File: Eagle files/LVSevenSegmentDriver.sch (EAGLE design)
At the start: 20 parts, among them IC1 74HC595D

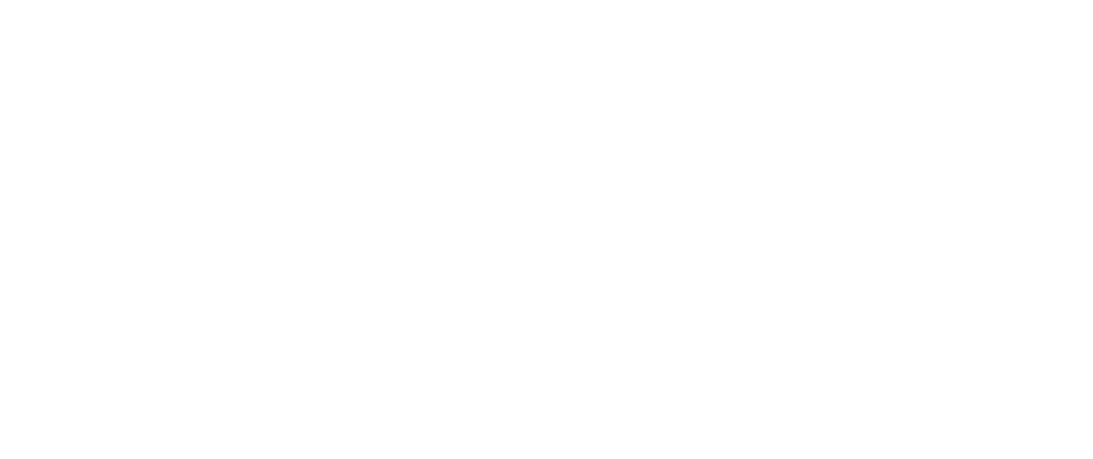
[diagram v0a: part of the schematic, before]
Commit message: Ready for Fabbing
Silk Screens added and last minute DRC checks done.
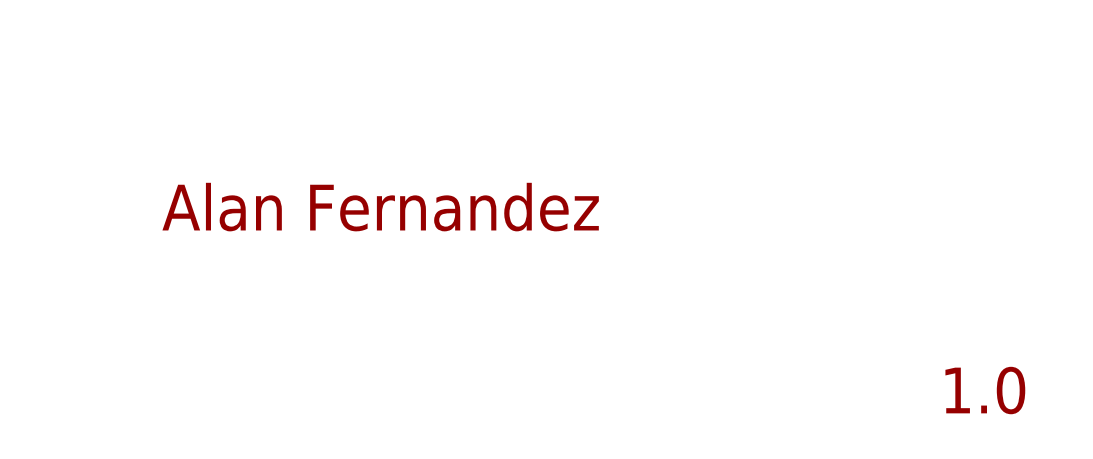
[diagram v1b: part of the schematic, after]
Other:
- note added: "1.0"
- note added: "Alan Fernandez"
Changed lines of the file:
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@@
 <part name="R7" library="SparkFun-Passives" deviceset="RESISTOR" device="1206" value="68"/>
 <part name="R8" library="SparkFun-Passives" deviceset="RESISTOR" device="1206" value="68"/>
+<part name="FRAME1" library="frames" deviceset="LETTER_L" device=""/>
 </parts>
 <sheets>
 <sheet>
 <plain>
+<text x="106.68" y="-40.64" size="5.08" layer="94">Alan Fernandez</text>
+<text x="193.04" y="-60.96" size="5.08" layer="94">1.0</text>
 </plain>
 <instances>
@@
 <instance part="R7" gate="G$1" x="132.08" y="27.94"/>
 <instance part="R8" gate="G$1" x="132.08" y="25.4"/>
+<instance part="FRAME1" gate="G$1" x="-43.18" y="-66.04"/>
+<instance part="FRAME1" gate="G$2" x="104.14" y="-66.04"/>
 </instances>
 <busses>

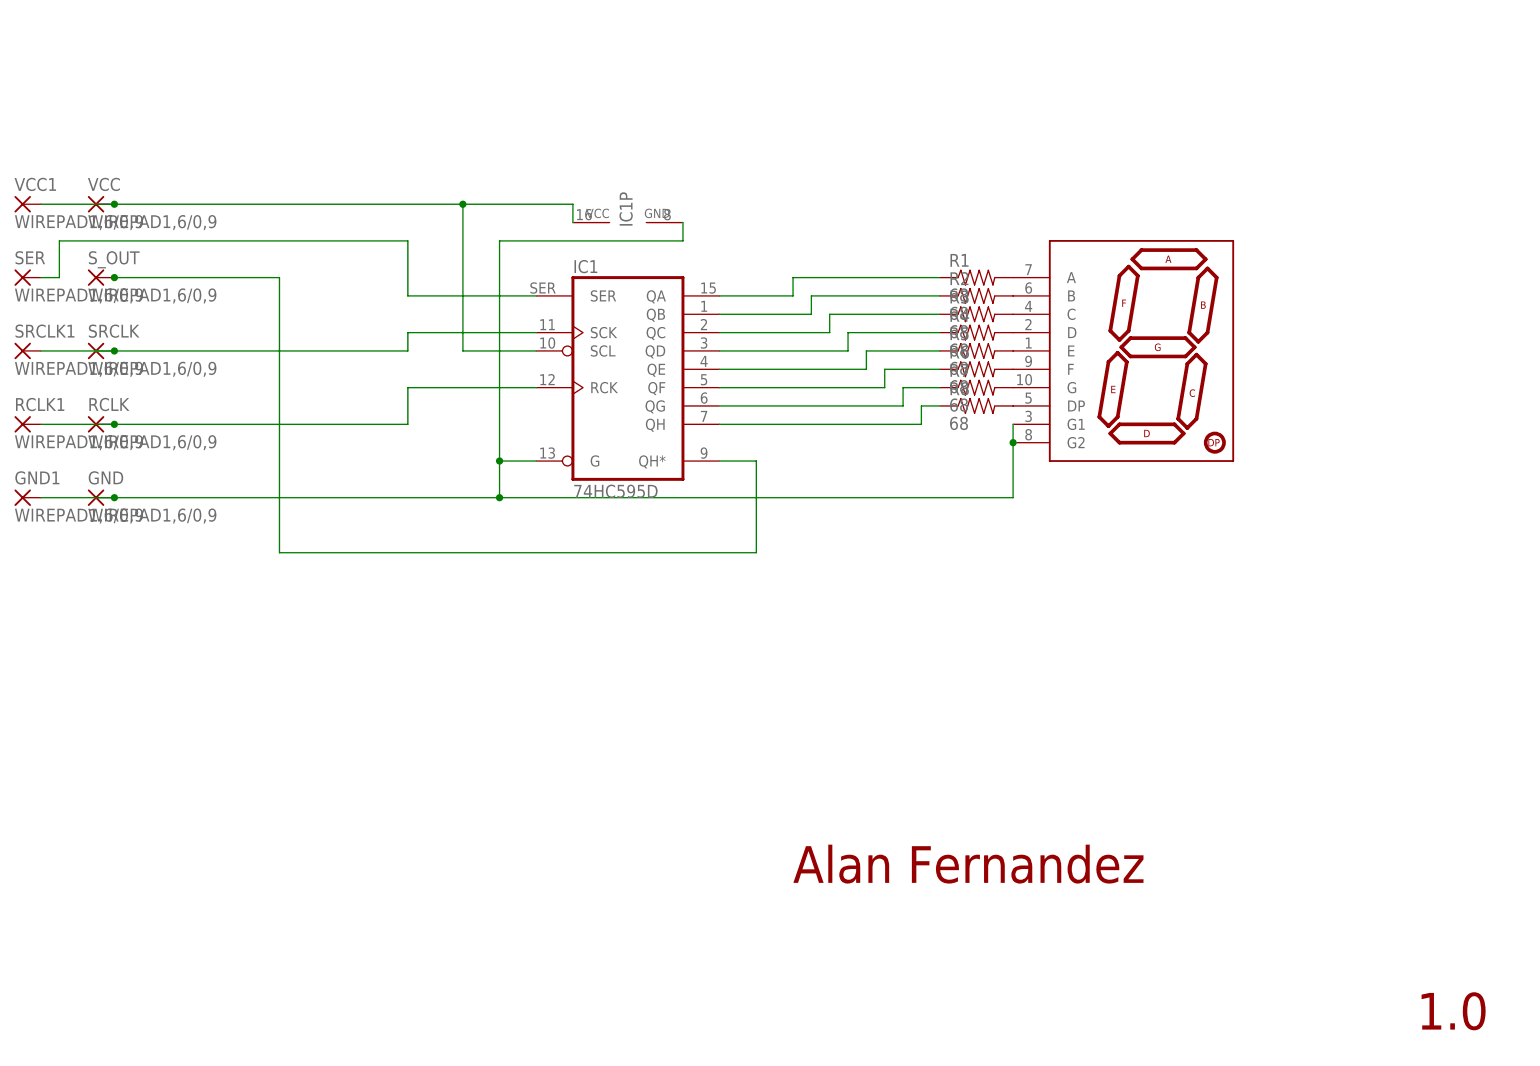
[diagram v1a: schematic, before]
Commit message: aaaaaaaaaaaaaaaaaaaaaaaaaaaaaaaaaaaa
Cleaned up schematics, replaced wire solder points with header pin
mounts for standardization, recreated a broken file and dealt with the
confusion and insanity that followed.
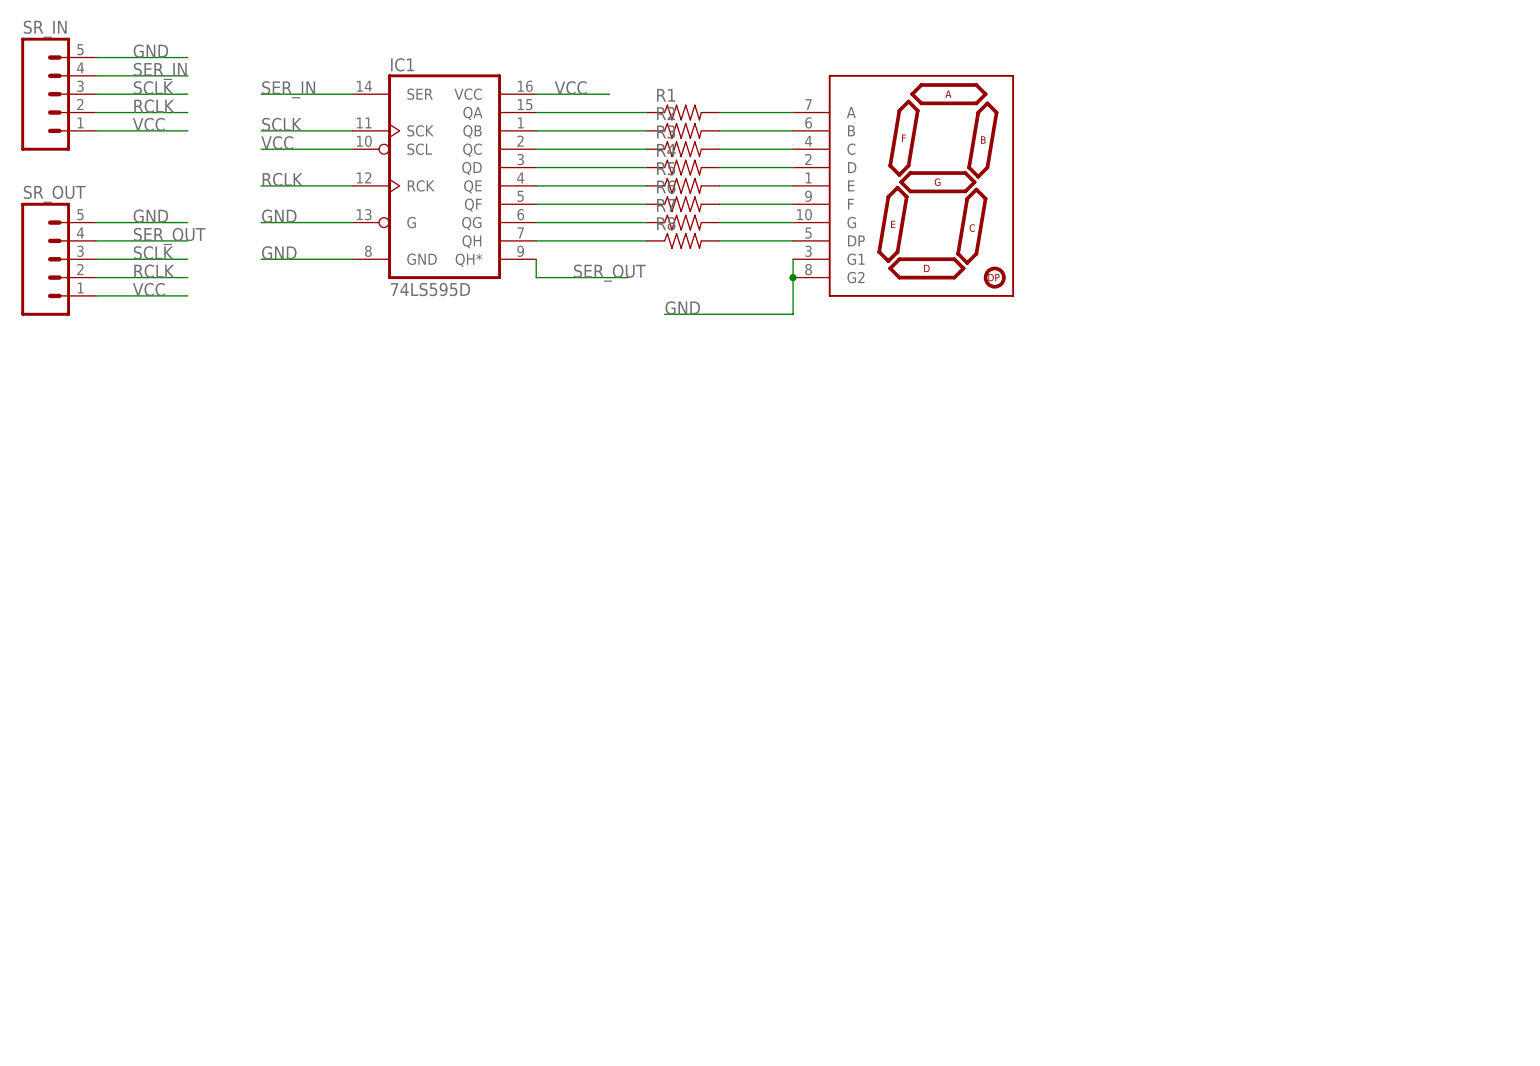
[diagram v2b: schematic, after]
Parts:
- removed GND, GND1, RCLK, RCLK1, SER, SRCLK, SRCLK1, S_OUT: WIREPAD1,6/0,9, wirepad:WIREPAD1,6/0,9
- removed VCC, VCC1: WIREPAD1,6/0,9, smallestWirepadSquare:WIREPAD1,6/0,9
- added SR_IN, SR_OUT: (no value), SparkFun-Connectors:M05PTH
- IC1: value 74HC595D -> 74LS595D; device 74xx-eu:74HC595D -> SparkFun-DigitalIC:74LS595D
- R1, R2, R3, R4, R5, R6, R7, R8: value 68 -> (none); device SparkFun-Passives:RESISTOR1206 -> SparkFun-Resistors:RESISTOR1206
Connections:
- removed net N$10 (its old number): IC1A.QH, R8.1
- removed net N$12 (its old number): IC1A.RCK, RCLK.P, RCLK1.P
- removed net N$14 (its old number): IC1A.SER, SER.P
- removed net N$4 (its old number): IC1A.QB, R2.1
- removed net N$6 (its old number): IC1A.QD, R4.1
- removed net N$8 (its old number): IC1A.QF, R6.1
- new net N$1: IC1.QA, R1.1
- new net N$15: IC1.QH, R8.1
- new net RCLK: IC1.RCK, SR_IN.2, SR_OUT.2
- new net SCLK: IC1.SCK, SR_IN.3, SR_OUT.3
- new net SER_IN: IC1.SER, SR_IN.4
- new net SER_OUT: IC1.QH*, SR_OUT.4
- net GND: now also IC1.G, IC1.GND, SR_IN.5, SR_OUT.5; no longer GND.P, GND1.P, IC1A.G, IC1P.GND
- net N$11: now also IC1.QF, R6.1; no longer IC1A.QH*, S_OUT.P
- net N$13: now also IC1.QG, R7.1; no longer IC1A.SCK, SRCLK.P, SRCLK1.P
- net N$3: now also IC1.QB, R2.1; no longer IC1A.QA, R1.1
- net N$5: now also IC1.QC; no longer IC1A.QC
- net N$7: now also IC1.QD, R4.1; no longer IC1A.QE, R5.1
- net N$9: now also IC1.QE, R5.1; no longer IC1A.QG, R7.1
- net VCC: now also IC1.SCL, IC1.VCC, SR_IN.1, SR_OUT.1; no longer IC1A.SCL, IC1P.VCC, VCC.P, VCC1.P
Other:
- note removed: "1.0"
- note removed: "Alan Fernandez"
- moved on the sheet: R1, R2, R3, R4, R5, R6, R7, R8
